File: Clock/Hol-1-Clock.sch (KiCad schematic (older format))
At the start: 18 parts, among them P1 CONN_2, P2 CONN_1, P3 CONN_1, SW1 SW_PUSH, U1 NE555, U2 NE555

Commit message: v1.4.3 added schematic for clock selection
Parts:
- added C6, C7: 100nF, ~, symbol C
- added D2: LED, ~, symbol LED
- added P4, P5, P6: CONN_2, ~, symbol CONN_2
- added R6, R7: 1kΩ, ~, symbol R
- added SW2: SPDT, ~, symbol SPDT
- added U3: NE555, ~, symbol NE555
- added U4: 74LS00, ~, symbol 74LS00
- added U5: 74LS04, ~, symbol 74LS04
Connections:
- net +5V: now also C7.1, P6.1 (P1), R6.1, R7.1, U3.8 (Vcc), U4.14 (+5V), U5.14 (+5V)
- net GND: now also C6.2, C7.2, D2.2 (K), P6.2 (PM), SW2.2, U3.1 (GND), U3.6 (THR), U4.7 (GND), U5.7 (GND)
- new net: U3.3 (OUT), U4.1, U5.5
- new net: P5.1 (P1), U4.2
- new net: U4.10, U4.3
- new net: P5.2 (PM), U4.4
- new net: U4.5, U5.6
- new net: U4.6, U4.9
- new net: U4.12, U4.8
- new net: U4.11, U5.11
- new net: U4.13, U5.8
- new net: P4.2 (PM), U5.9
- new net: D2.1 (A), P4.1 (P1), U5.10
- new net: R6.2, SW2.3, U3.2 (TRIG)
- new net: R7.2, SW2.1, U3.4 (~RESET)
- new net: C6.1, U3.5 (CTRL)
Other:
- note added: "555 Astable Output\nclock pulse frequency adjusted by RV1"
- note added: "555 Monostable Output\na debounced pulse when SW1 is pressed"
- note added: "555 to debounce SW2"
- note added: "CLOCK CONTROL circuit (below). Choose between source A or B above or connect external sources"
- note added: "Clock output"
- note added: "Clock source\ninputs A & B"
- note added: "Halt control\n(stop the clock)\n"
- note added: "Select input A or B"
- note removed: "Astable Output\nclock pulse frequency adjusted by RV1"
- note removed: "Monostable Output\na debounced pulse when SW1 is pressed"
- moved on the sheet: C1, C2, C3, C4, C5, D1, P1, P2, P3, R1, R2, R3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

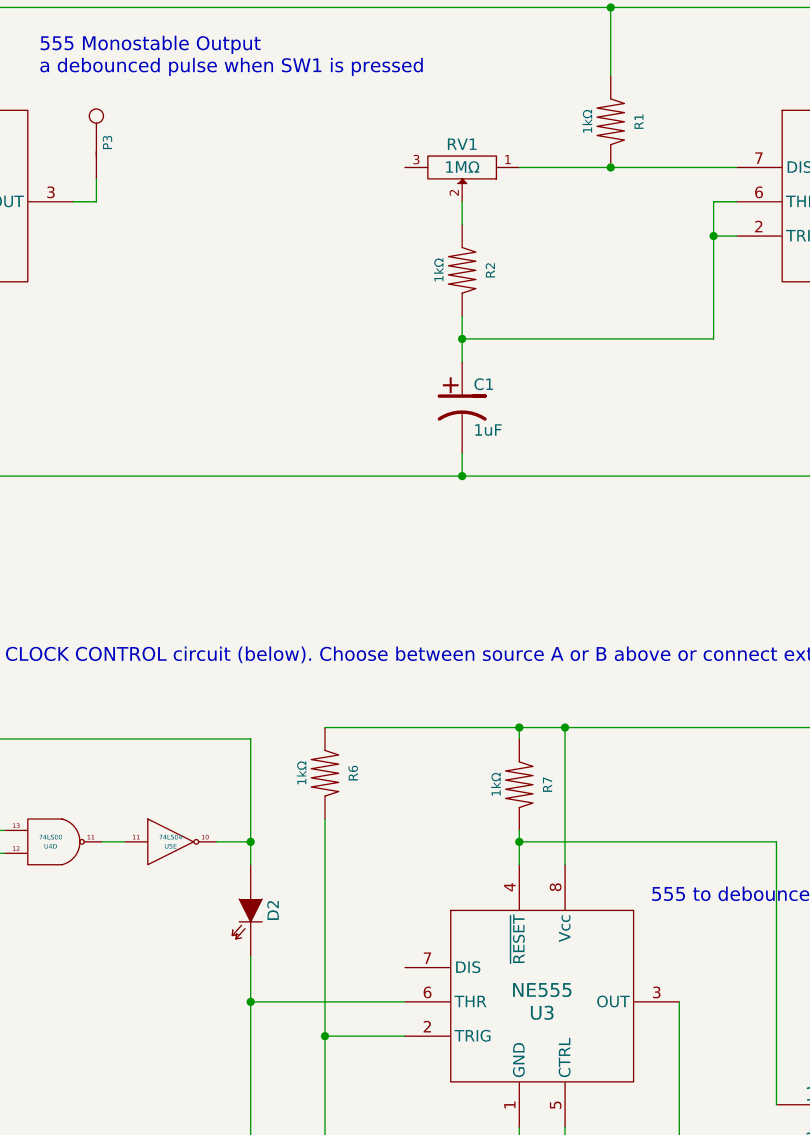
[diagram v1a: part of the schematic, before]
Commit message: v1.4.4 added PCB for clock selection
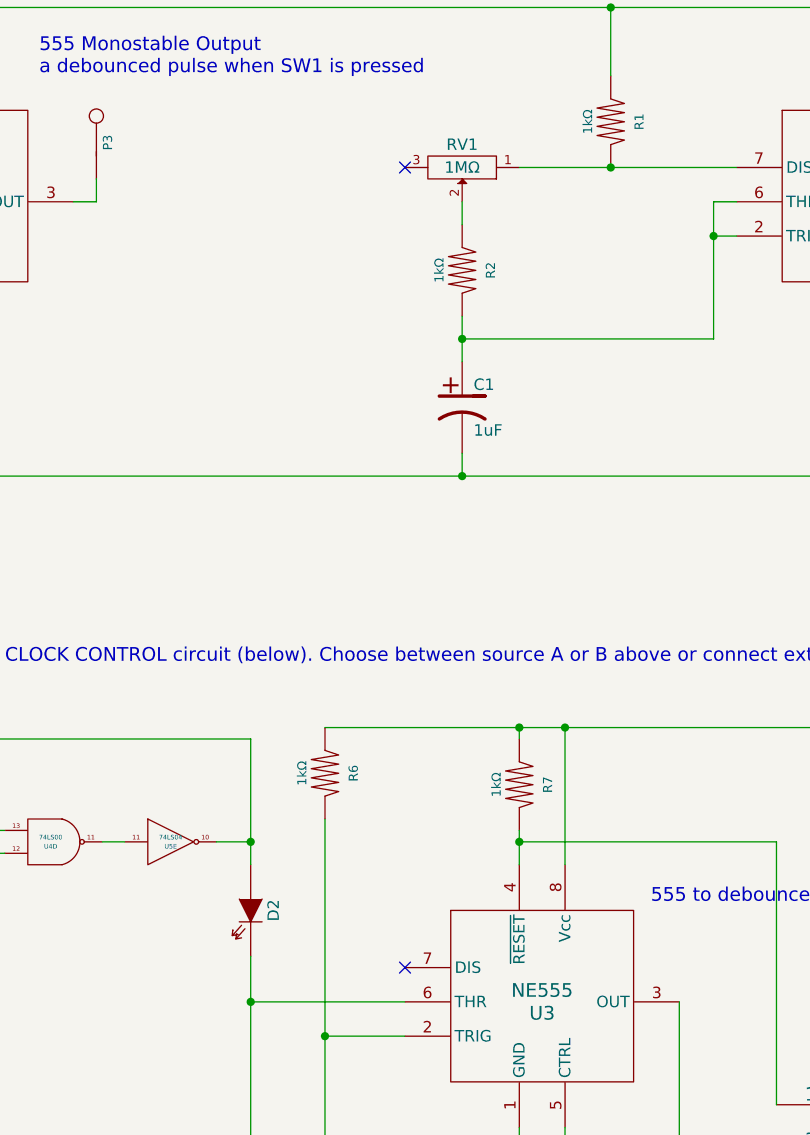
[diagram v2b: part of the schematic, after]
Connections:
- no-connect marks 0 -> 2
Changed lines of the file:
@@
 Sheet 1 1
 Title "Hol-1 8-bit CPU clock source & selection"
-Date "31 mar 2019"
+Date "5 apr 2019"
 Rev ""
 Comp "www.benningtons.net"
@@
 	5900 4150 5900 4100
 Connection ~ 5900 4100
+NoConn ~ 5400 5150
+NoConn ~ 5400 1650
 $EndSCHEMATC

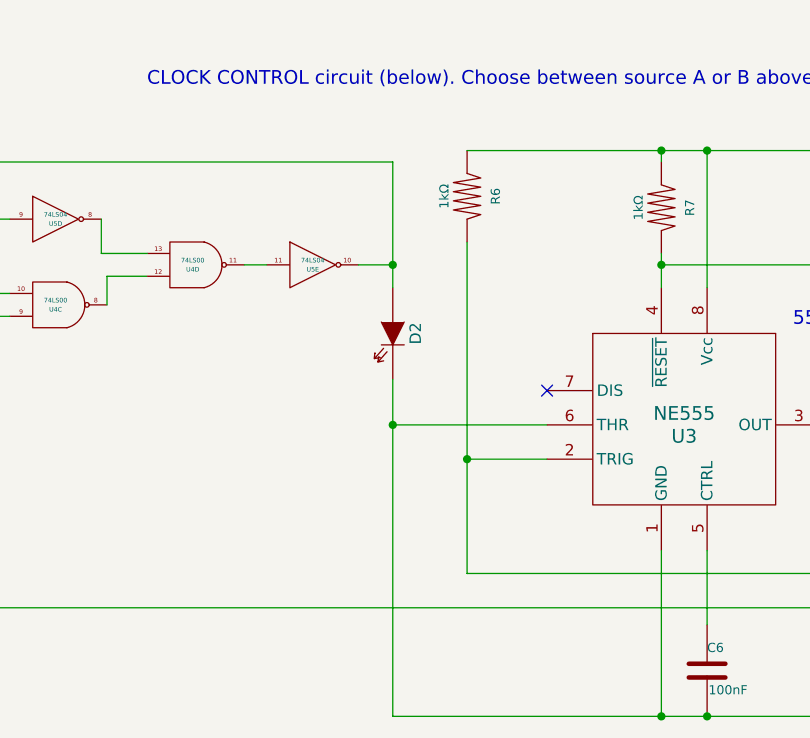
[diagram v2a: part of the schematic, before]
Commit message: v1.4.5 don't drive an LED directly from the clock output
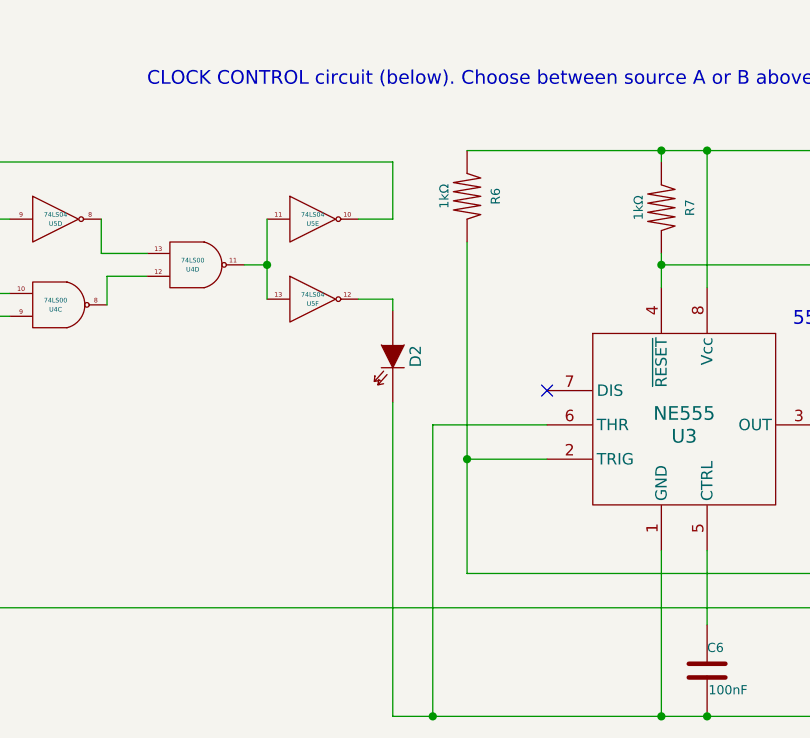
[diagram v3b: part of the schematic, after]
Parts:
- added unit 6 of U5
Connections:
- net at U4.11, U5.11: now also U5.13
- net at P4.1 (P1), U5.10: no longer D2.1 (A)
- new net: D2.1 (A), U5.12
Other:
- moved on the sheet: D2, U5E
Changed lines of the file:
@@
 Sheet 1 1
 Title "Hol-1 8-bit CPU clock source & selection"
-Date "5 apr 2019"
+Date "23 apr 2019"
 Rev ""
 Comp "www.benningtons.net"
@@
 L 74LS04 U5
 U 5 1 5C9FF7BB
-P 4375 4600
-F 0 "U5" H 4375 4580 20  0000 C CNN
-F 1 "74LS04" H 4375 4620 20  0000 C CNN
-F 2 "~" H 4425 4600 60  0000 C CNN
-F 3 "~" H 4425 4600 60  0000 C CNN
-	5    4375 4600
+P 4375 4400
+F 0 "U5" H 4375 4380 20  0000 C CNN
+F 1 "74LS04" H 4375 4420 20  0000 C CNN
+F 2 "~" H 4425 4400 60  0000 C CNN
+F 3 "~" H 4425 4400 60  0000 C CNN
+	5    4375 4400
 	1    0    0    -1
 $EndComp
@@
 L LED D2
 U 1 1 5C9FFD86
-P 4725 4900
-F 0 "D2" H 4725 5000 50  0000 C CNN
-F 1 "LED" H 4725 4800 50  0001 C CNN
-F 2 "~" H 4725 4900 60  0000 C CNN
-F 3 "~" H 4725 4900 60  0000 C CNN
-	1    4725 4900
+P 4725 5000
+F 0 "D2" H 4725 5100 50  0000 C CNN
+F 1 "LED" H 4725 4900 50  0001 C CNN
+F 2 "~" H 4725 5000 60  0000 C CNN
+F 3 "~" H 4725 5000 60  0000 C CNN
+	1    4725 5000
 	0    1    1    0
 $EndComp
@@
 	1250 1200 1250 950
 Wire Wire Line
-	4075 4600 4175 4600
-Wire Wire Line
 	6100 5850 6100 6175
 Wire Wire Line
@@
 	5050 5950 7025 5950
 Wire Wire Line
-	4725 4600 4575 4600
-Connection ~ 4725 4600
-Wire Wire Line
 	3450 4400 3450 4550
 Wire Wire Line
@@
 	4725 6575 9175 6575
 Wire Wire Line
-	5400 5300 4725 5300
-Connection ~ 4725 5300
-Wire Wire Line
-	4725 5100 4725 6575
+	4725 5200 4725 6575
 Connection ~ 5900 6575
 Wire Wire Line
@@
 	2150 4150 4725 4150
 Wire Wire Line
-	4725 4150 4725 4700
-Wire Wire Line
 	5900 4550 5900 4700
 Wire Wire Line
@@
 NoConn ~ 5400 5150
 NoConn ~ 5400 1650
+$Comp
+L 74LS04 U5
+U 6 1 5CBF52F2
+P 4375 4750
+F 0 "U5" H 4375 4730 20  0000 C CNN
+F 1 "74LS04" H 4375 4770 20  0000 C CNN
+F 2 "~" H 4425 4750 60  0000 C CNN
+F 3 "~" H 4425 4750 60  0000 C CNN
+	6    4375 4750
+	1    0    0    -1
+$EndComp
+Wire Wire Line
+	4575 4750 4725 4750
+Wire Wire Line
+	4575 4400 4725 4400
+Wire Wire Line
+	4725 4750 4725 4800
+Wire Wire Line
+	4725 4400 4725 4150
+Wire Wire Line
+	4175 4400 4175 4750
+Wire Wire Line
+	4075 4600 4175 4600
+Connection ~ 4175 4600
+Wire Wire Line
+	5400 5300 4900 5300
+Wire Wire Line
+	4900 5300 4900 6575
+Connection ~ 4900 6575
 $EndSCHEMATC

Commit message: v1.5.19 upgraded to KiCad 5.0
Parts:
- C1: symbol CP1 -> benningtons:CP1
- C2, C3, C4, C5, C6, C7: symbol C -> benningtons:C
- D1, D2: symbol LED -> benningtons:LED
- P1, P4, P5, P6: symbol CONN_2 -> benningtons:CONN_2
- P2, P3: symbol CONN_1 -> benningtons:CONN_1
- R1, R2, R3, R4, R5, R6, R7: symbol R -> benningtons:R
- RV1: symbol POT -> benningtons:POT
- SW1: symbol SW_PUSH -> benningtons:SW_PUSH
- SW2: symbol SPDT -> benningtons:SPDT
- U1, U2, U3: symbol NE555 -> benningtons:NE555
- U4: symbol 74LS00 -> benningtons:74LS00
- U5: symbol 74LS04 -> benningtons:74LS04
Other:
- moved on the sheet: C6, C7, D2, P4, P5, P6, R6, R7, SW2, U3, U4A, U4B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
